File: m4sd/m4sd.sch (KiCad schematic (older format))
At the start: 34 parts

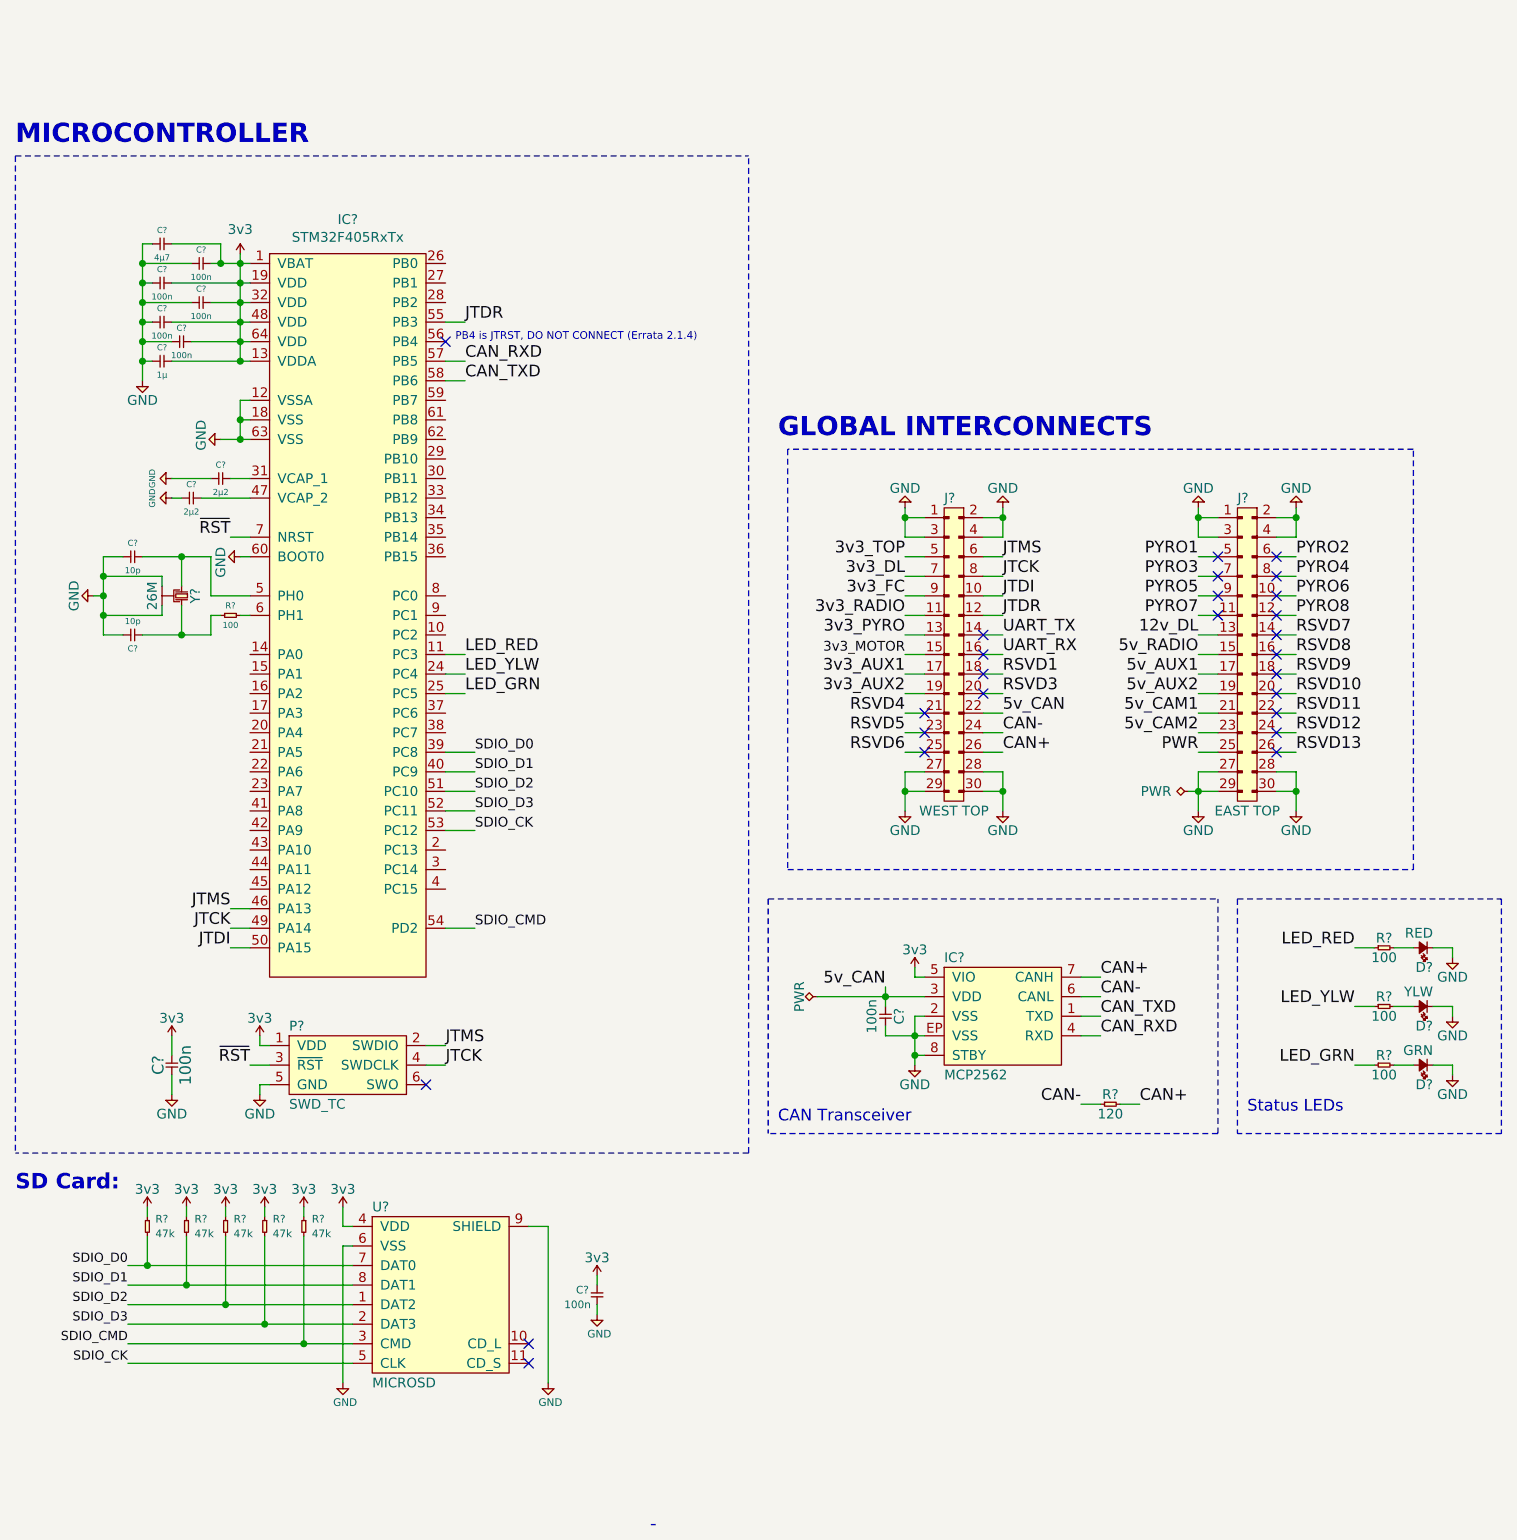
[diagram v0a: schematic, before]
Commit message: Update SD schematic layout
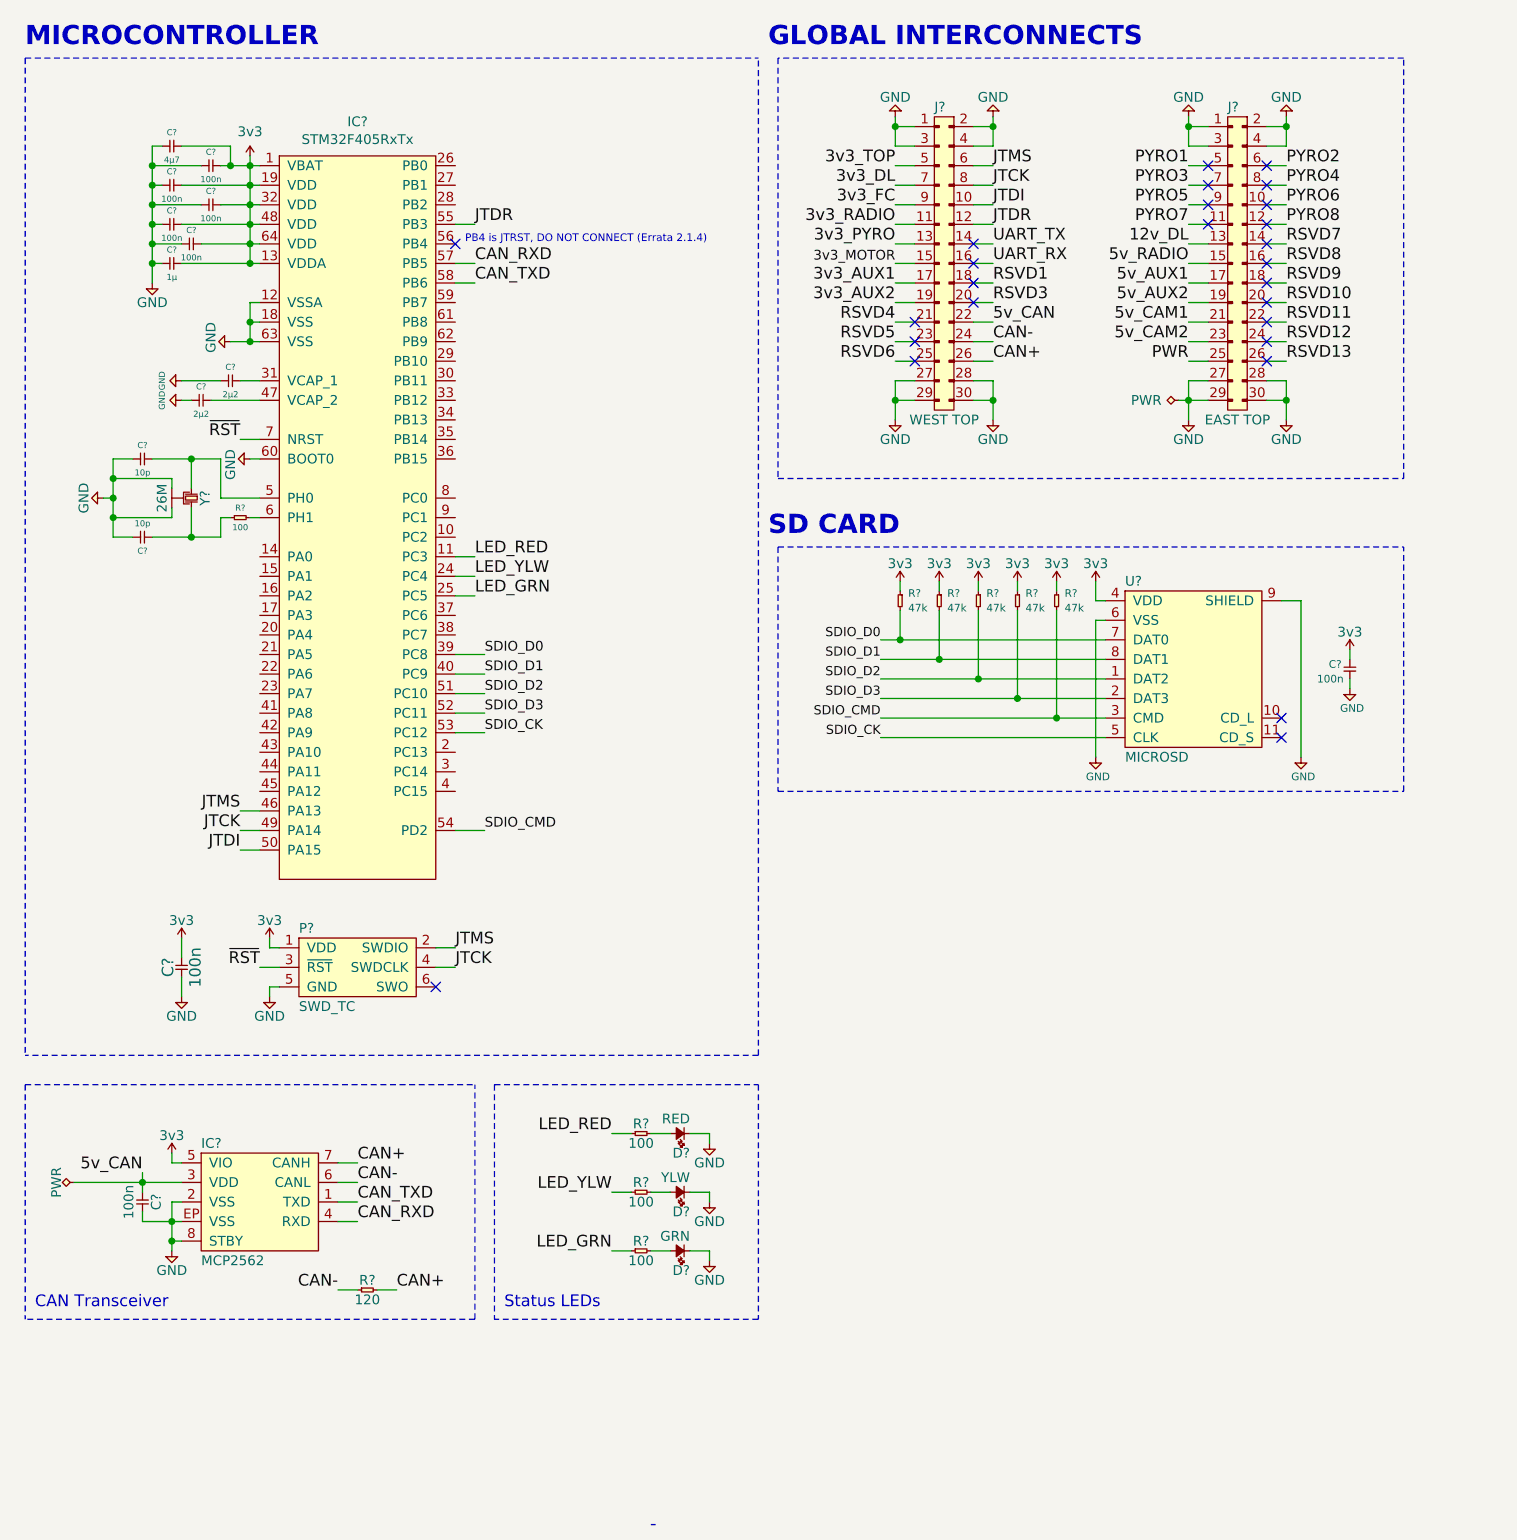
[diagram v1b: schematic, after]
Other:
- note added: "SD CARD"
- note removed: "SD Card:"
- moved on the sheet: C?, D?, IC?, J?, P?, R?, U?, Y?

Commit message: Use cusf-kicad.lib instead of agg-kicad.lib
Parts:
- C? (x14): symbol agg-kicad:C -> cusf-kicad:C
- D? (x3): symbol agg-kicad:LED -> cusf-kicad:LED
- IC?: symbol agg-kicad:STM32F405RxTx -> cusf-kicad:STM32F405RxTx
- IC?: symbol agg-kicad:MCP2562 -> cusf-kicad:MCP2562
- J? (x2): symbol agg-kicad:CONN_02x15 -> cusf-kicad:CONN_02x15
- P?: symbol agg-kicad:SWD_TC -> cusf-kicad:SWD_TC
- R? (x10): symbol agg-kicad:R -> cusf-kicad:R
- U?: symbol agg-kicad:MICROSD -> cusf-kicad:MICROSD
- Y?: symbol agg-kicad:SMD_XTAL -> cusf-kicad:SMD_XTAL
